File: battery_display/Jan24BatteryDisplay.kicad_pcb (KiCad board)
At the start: 2 copper layers, 90 x 60 mm, 25 parts, among them J1 FH34SRJ-24S-0.5SH_99_, J2 Screw_Terminal_2x2.54, Q2 ZXM61N03F, SW1 Button

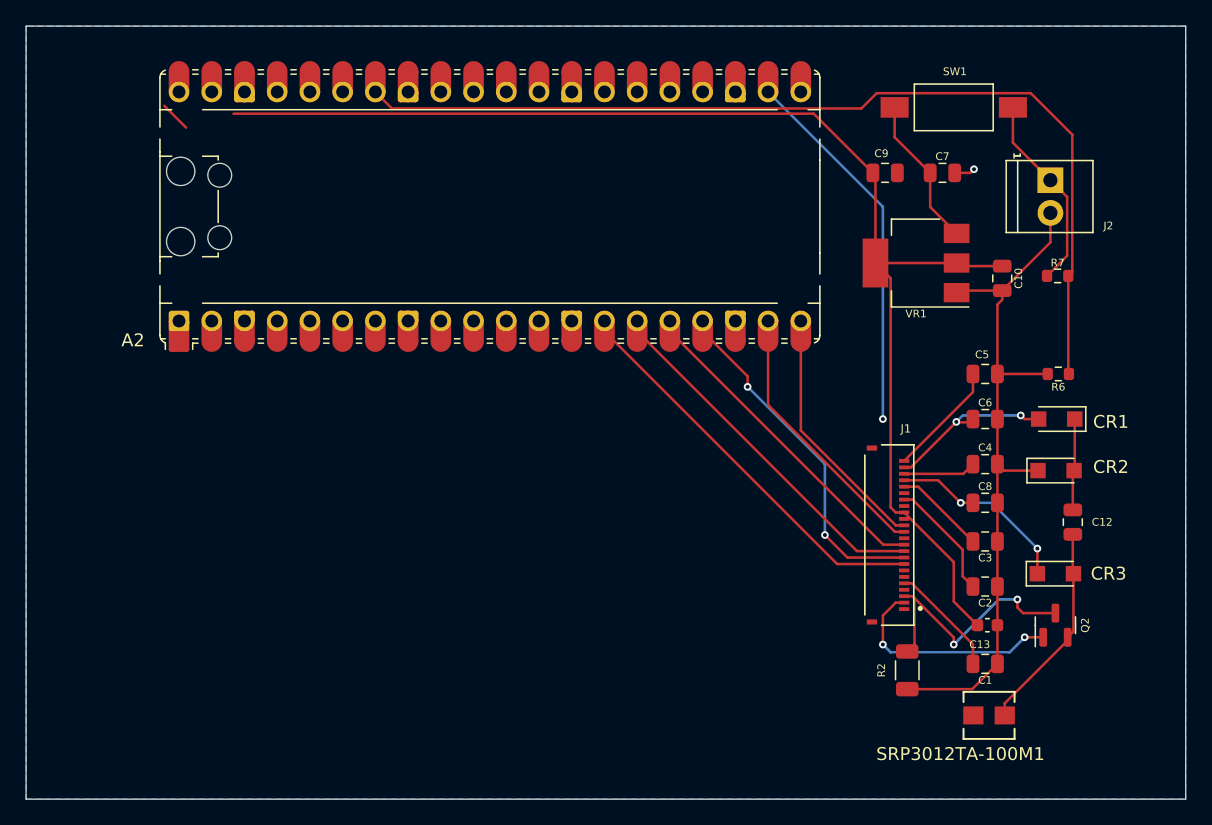
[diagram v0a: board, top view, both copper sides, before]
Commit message: update schematic
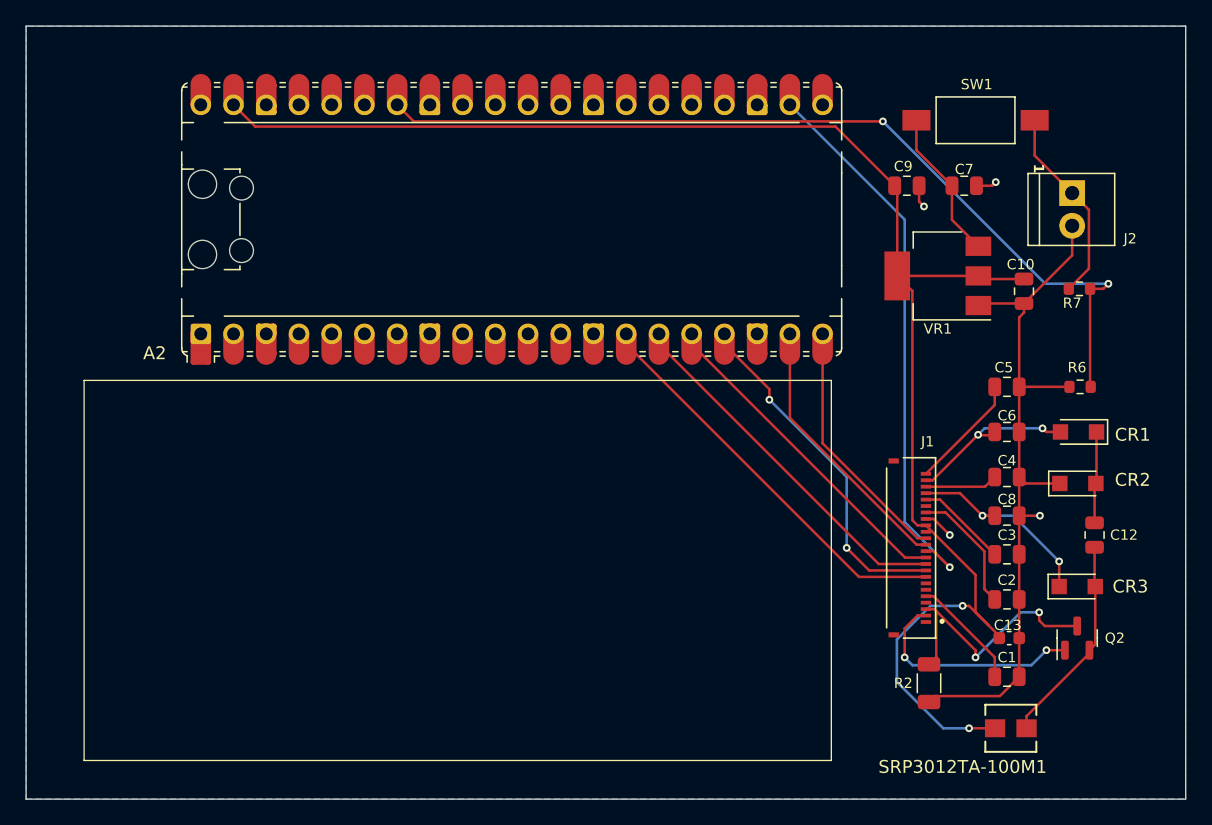
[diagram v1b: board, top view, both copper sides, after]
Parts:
- moved A2 1.96 mm to (377.2, 49.0)
- moved C1 1.96 mm to (415.6, 84.5)
- moved C10 1.96 mm to (417.0, 54.6)
- moved C12 1.96 mm to (422.4, 73.5)
- moved C13 1.96 mm to (415.8, 81.5)
- moved C2 1.96 mm to (415.6, 78.5)
- moved C3 1.96 mm to (415.6, 75.0)
- moved C4 1.96 mm to (415.6, 69.0)
- moved C5 1.96 mm to (415.6, 62.0)
- moved C6 1.96 mm to (415.6, 65.5)
- moved C7 1.96 mm to (412.3, 46.4)
- moved C8 1.96 mm to (415.6, 72.0)
- moved C9 1.96 mm to (407.9, 46.4)
- moved CR1 1.96 mm to (421.2, 65.5)
- moved CR2 1.96 mm to (421.1, 69.5)
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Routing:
- net +3.3V: track 102.5 -> 123.7 mm, vias 0 -> 2
- net CSB: track 29.1 -> 43.4 mm
- net GND: track 56.5 -> 62.2 mm, vias 1 -> 4
- net Net-(A2-GPIO28_ADC2): track 75.2 -> 70.6 mm, vias 0 -> 2
- net BUSY_N: track 27.8 -> 26.6 mm
- net Net-(C2-Pad2): track 9.34 -> 9.85 mm
